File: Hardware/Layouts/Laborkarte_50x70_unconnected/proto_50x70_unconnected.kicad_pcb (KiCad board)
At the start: 2 copper layers, 50 x 70 mm, 290 parts

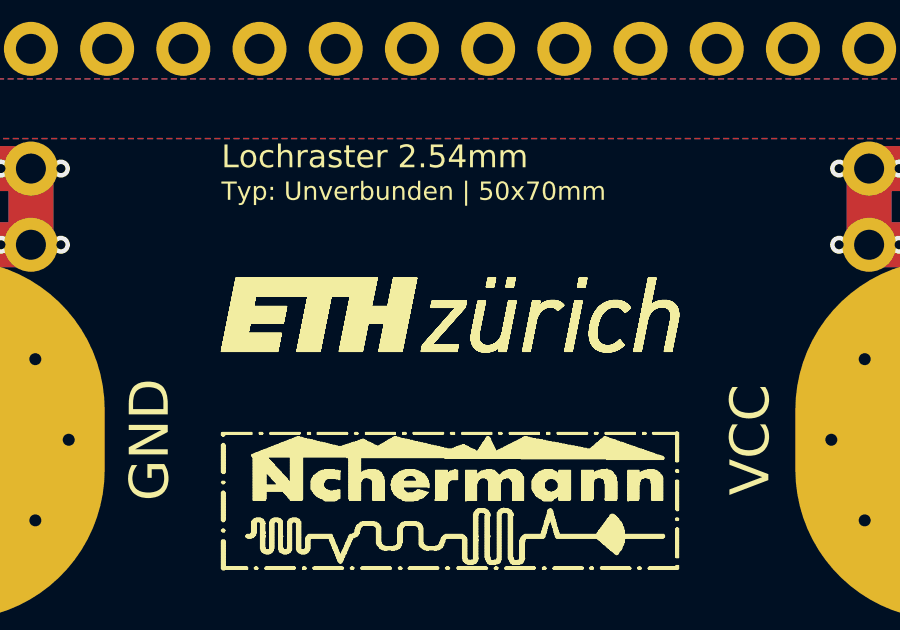
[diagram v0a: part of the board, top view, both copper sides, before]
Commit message: Fix ETH logo visibility, add violet PCB background, show F+B sides
- Downscale high-res logo images before rasterizing so line width
  stays visible (ETH logo was 0.005mm, now 0.02mm)
- Preview images now show front and back side by side
- Board background changed to JLCPCB violet
- PDF updated with filled copper zones and fixed silkscreen parsing
- All Gerbers and ZIPs regenerated
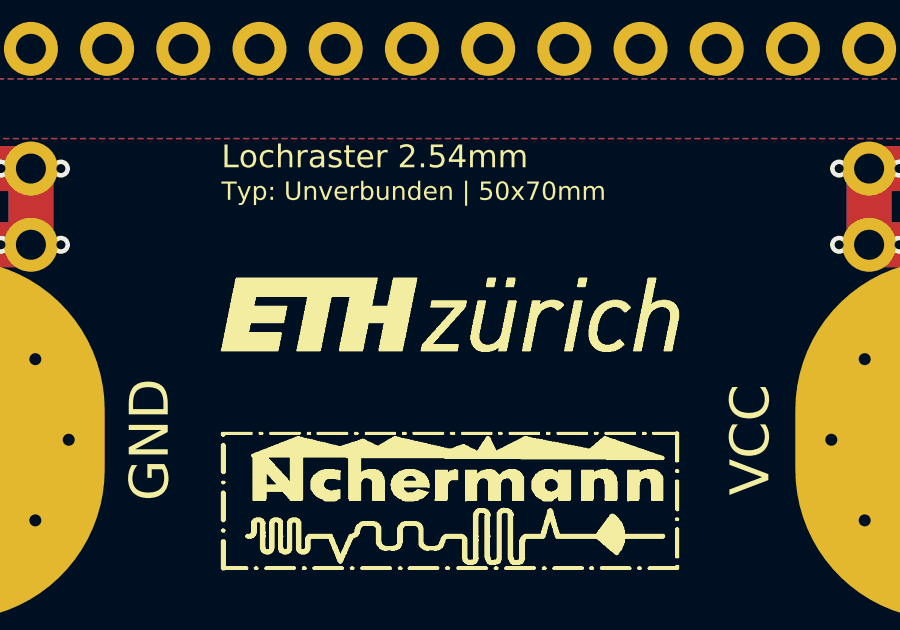
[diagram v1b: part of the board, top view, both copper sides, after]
